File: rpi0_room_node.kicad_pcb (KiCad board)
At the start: 2 copper layers, 65 x 30 mm, 35 parts, among them IC1 DS2482-100S, J1 Raspberry Pi, J2 Conn_01x03, J3 Conn_01x03, U1 ADS1015IDGS, U2 DS18B20, U3 DS18B20

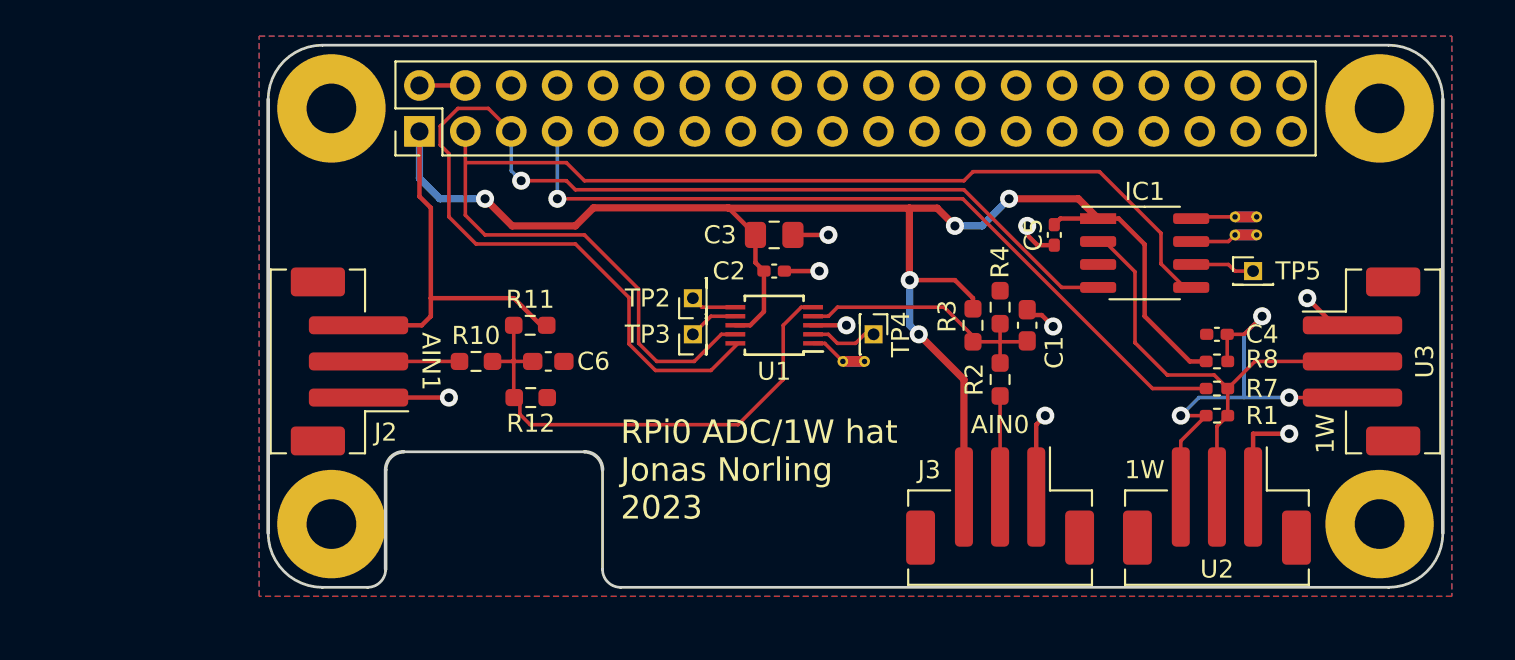
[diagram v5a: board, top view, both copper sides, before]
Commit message: Add 2.54 mm holes to JST connectors
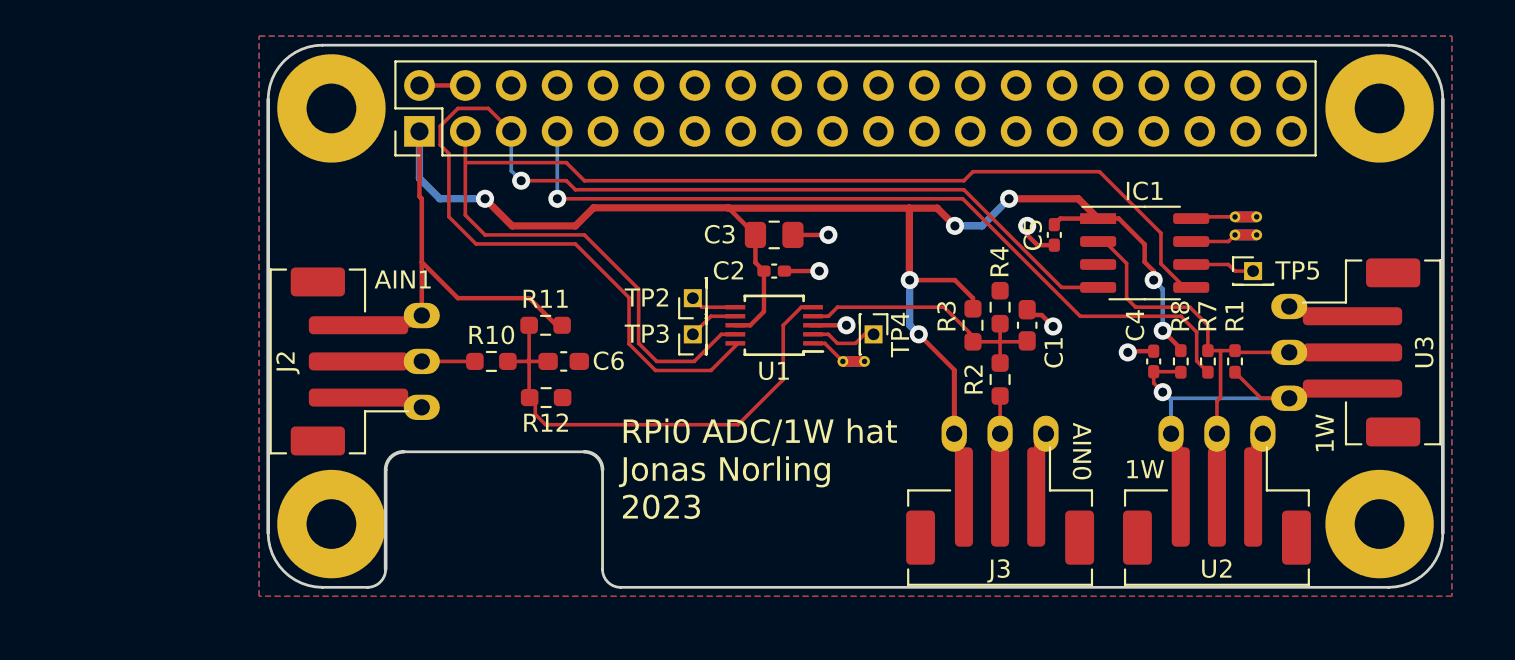
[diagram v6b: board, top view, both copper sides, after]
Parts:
- J2, J3, U2, U3: footprint Connector_JST:JST_PH_B3B-PH-SM4-TB_1x03-1MP_P2.00mm_Vertical -> weird connectors:JST_PH_B3B-PH-SM4-TB_1x03-1MP_P2.00mm_Vertical + 2.54 mm header
- moved C4 3.81 mm to (145.5, 114.0), turned to -90 degrees
- moved R1 3.16 mm to (150.0, 114.0), turned to 90 degrees
- moved R8 2.00 mm to (147.0, 114.0), turned to -90 degrees
- moved R7 1.58 mm to (148.5, 114.0), turned to 90 degrees
- moved C6 0.85 mm to (112.9, 114.0)
- moved R10 0.85 mm to (108.9, 114.0)
- moved R11 0.85 mm to (111.9, 112.0)
- moved R12 0.85 mm to (111.9, 116.0)
- moved U3 0.50 mm to (157.0, 113.5)
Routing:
- net GND: track 27.2 -> 18.8 mm, vias 9 -> 6
- net /1W_VDD: track 25.1 -> 19.2 mm, vias 3 -> 1
- net /ONEWIRE: track 26.2 -> 23.3 mm
- net /AIN1: track 28.2 -> 27.3 mm
- net Net-(J1-Pad7): track 43.8 -> 44.4 mm
- net +3.3V: vias 5 -> 7

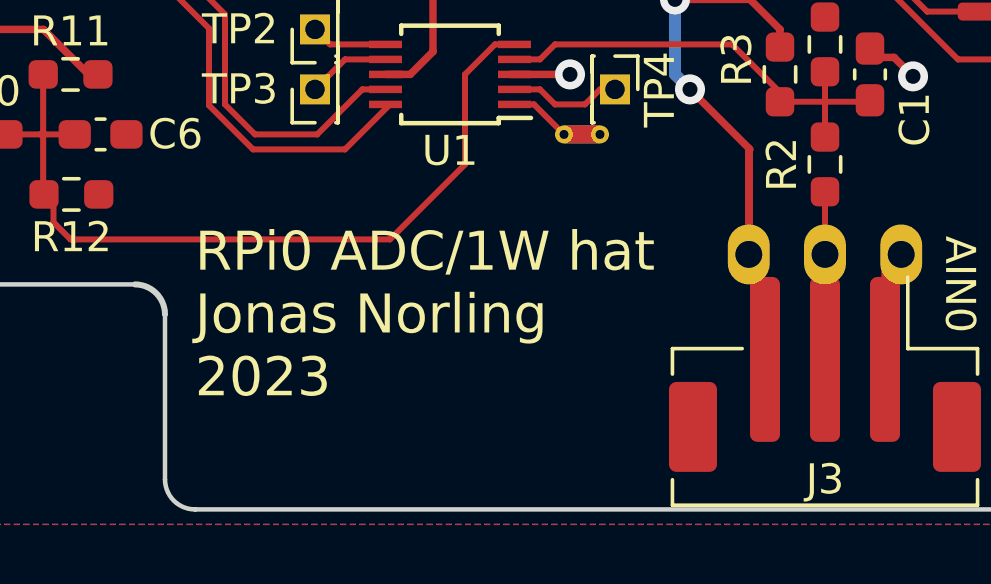
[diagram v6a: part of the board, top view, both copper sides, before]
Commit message: Move silkscreen texts
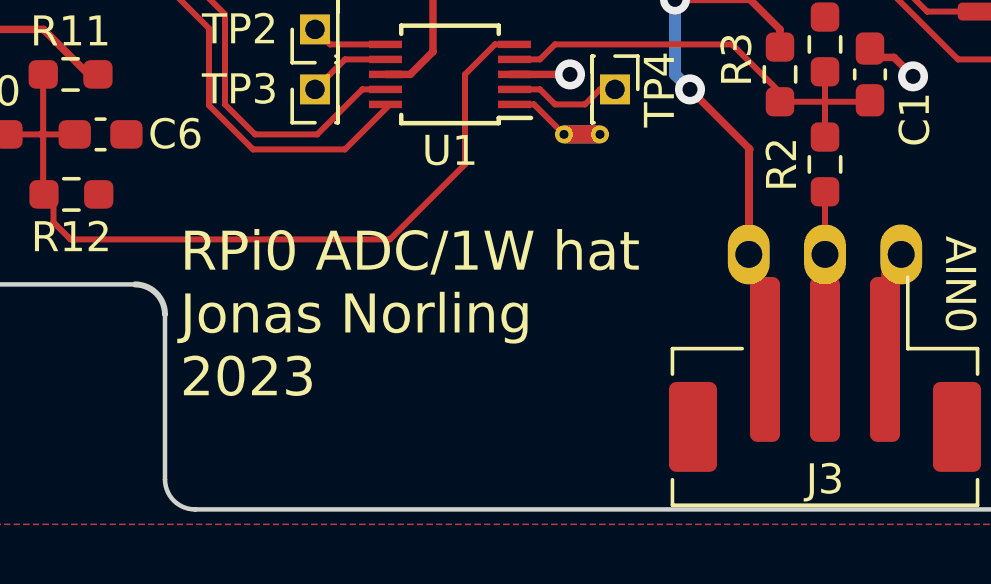
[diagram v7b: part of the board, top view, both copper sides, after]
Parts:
- moved G*** 16.2 mm to (135.2, 107.2)
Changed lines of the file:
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@@
   )
   (footprint "elemental:elemental-25.4mm" (layer "B.Cu")
-    (at 128.5 122 180)
+    (at 135.25 107.25 180)
     (attr through_hole)
     (fp_text reference "G***" (at 0 0) (layer "B.SilkS") hide
@@
     (effects (font (size 1 1) (thickness 0.2)))
   )
-  (gr_text "RPi0 ADC/1W hat\nJonas Norling\n2023" (at 116 120) (layer "F.SilkS")
+  (gr_text "RPi0 ADC/1W hat\nJonas Norling\n2023" (at 115.5 120) (layer "F.SilkS")
     (effects (font (size 1.3 1.3) (thickness 0.25)) (justify left))
   )
